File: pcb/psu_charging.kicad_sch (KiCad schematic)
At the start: 22 parts, among them J1 BATT+, J2 GND, J4 VBUS, J6 S2B-PH-K/DNP, J7 GND, J8 124018612112A, U1 AP2112K-3.3, U4 MCP73831/OT

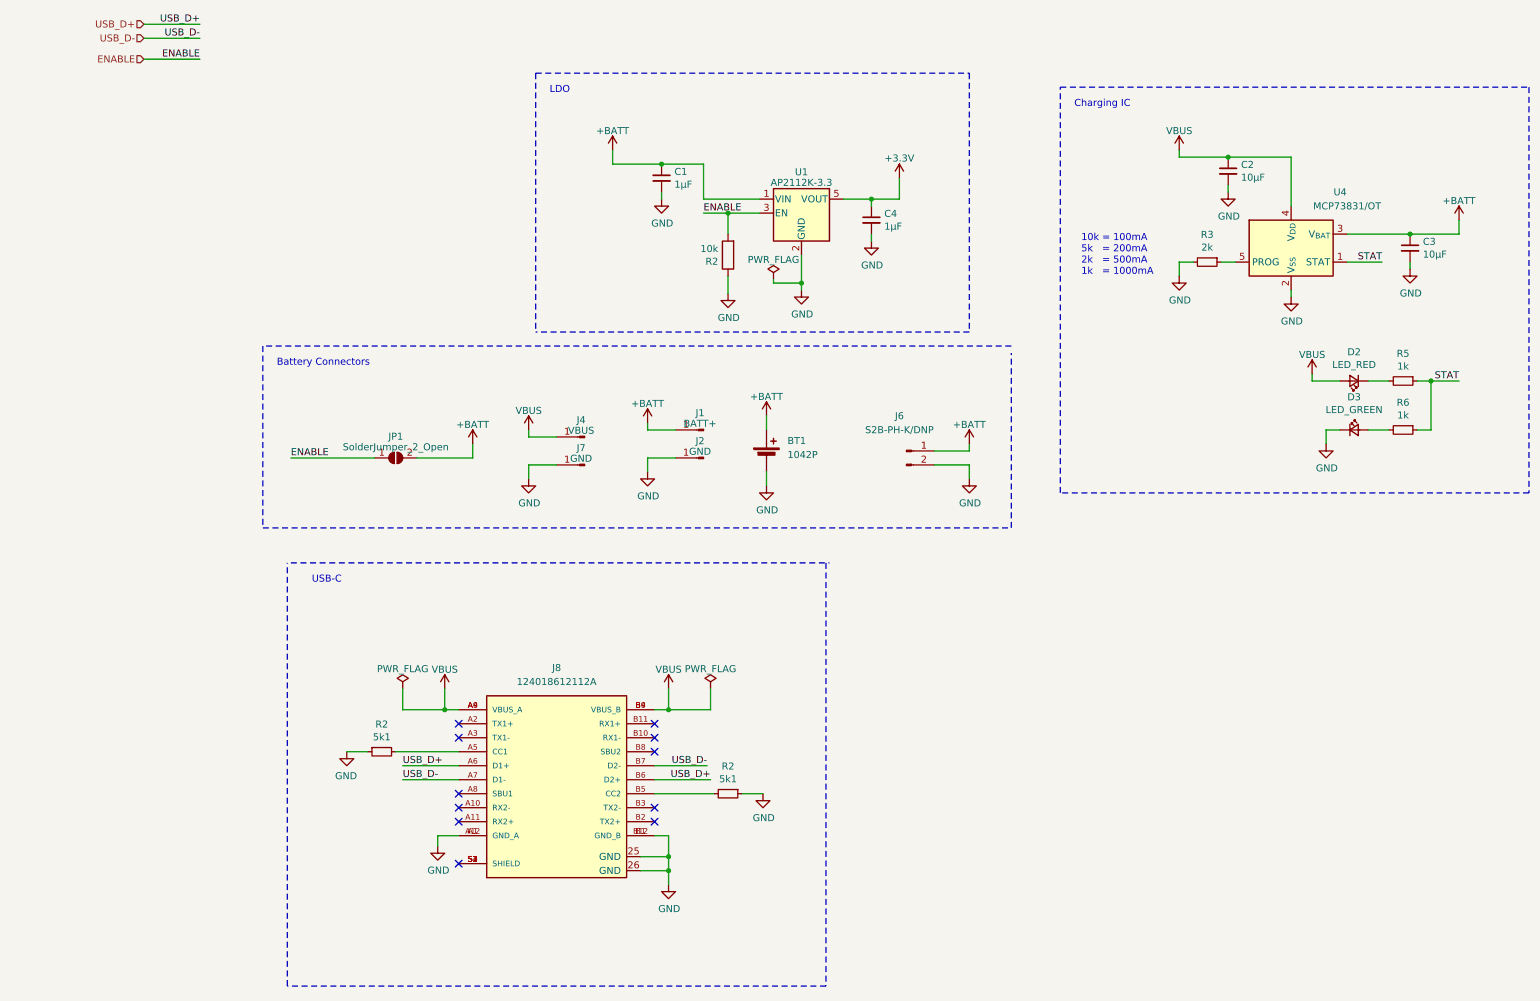
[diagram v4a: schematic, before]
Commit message: re-organise components + added housing data
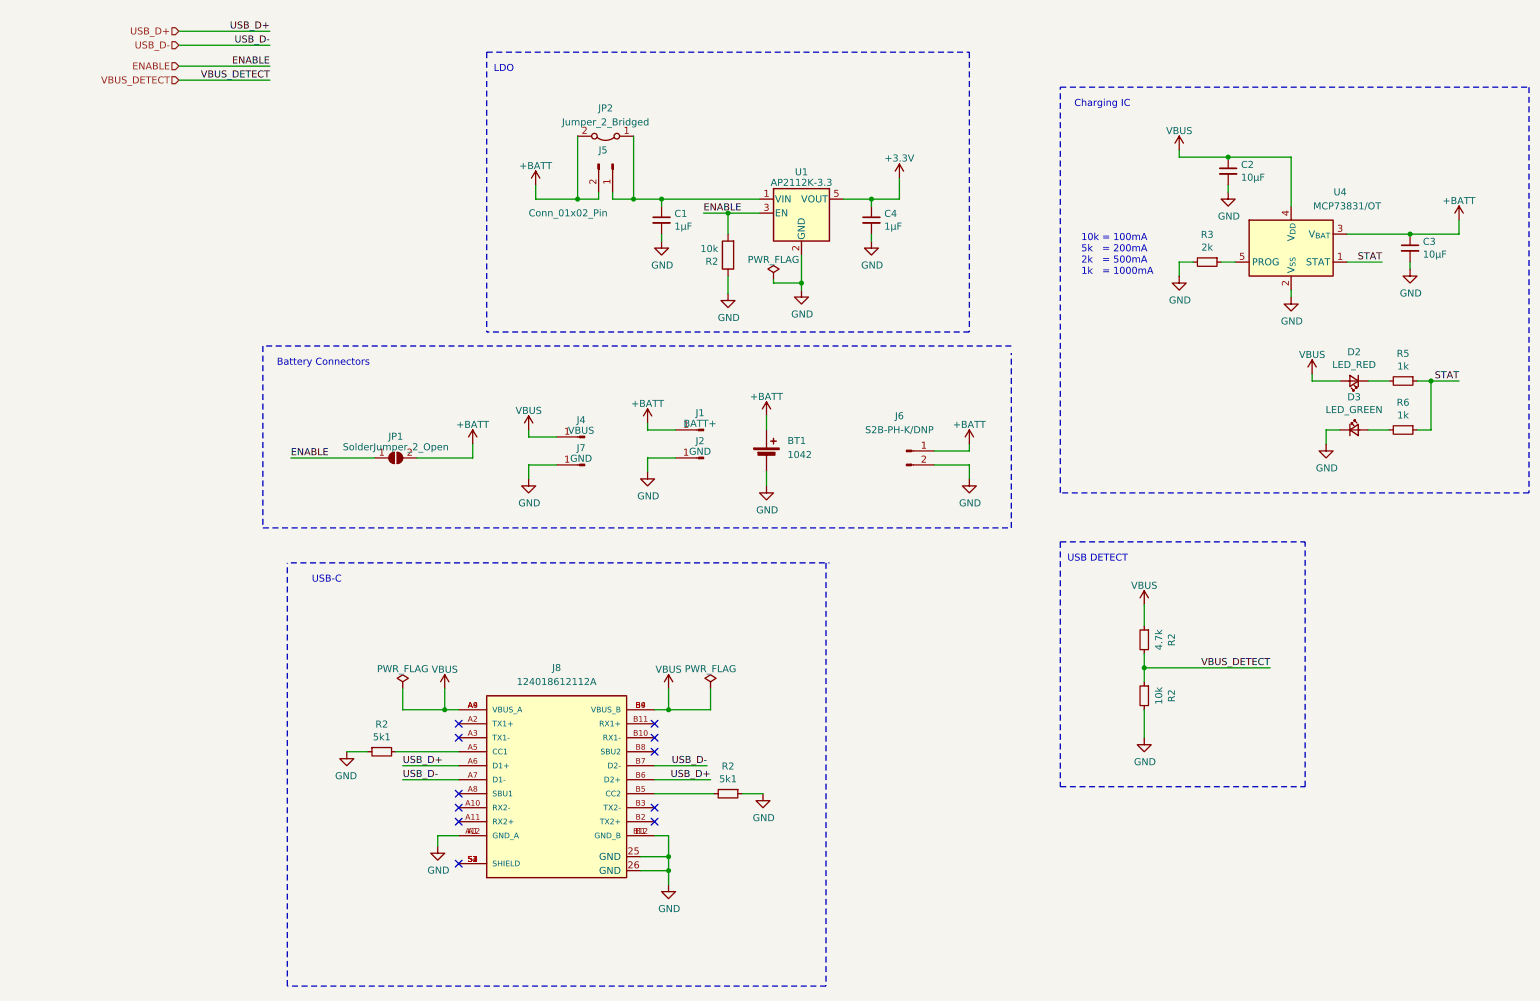
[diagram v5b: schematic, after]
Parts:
- added J5: Conn_01x02_Pin, Connector_PinSocket_2.54mm:PinSocket_1x02_P2.54mm_Vertical, symbol Connector:Conn_01x02_Pin
- added JP2: Jumper_2_Bridged, Jumper:SolderJumper-2_P1.3mm_Bridged_RoundedPad1.0x1.5mm, symbol Jumper:Jumper_2_Bridged
- added R2: 4.7k, Resistor_SMD:R_0603_1608Metric, symbol Device:R_Small
- added R2: 10k, Resistor_SMD:R_0603_1608Metric, symbol Device:R_Small
- BT1: value 1042P -> 1042
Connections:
- net +BATT: now also J5.2 (Pin_2), JP2.2 (B); no longer C1.1, U1.1 (VIN)
- net GND: now also R2.2
- net VBUS: now also R2.1
- new net: C1.1, J5.1 (Pin_1), JP2.1 (A), U1.1 (VIN)
- new net VBUS_DETECT: R2.1, R2.2
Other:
- note added: "USB DETECT"
- moved on the sheet: C1

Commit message: Replaced RP2040 with ESP32 + Schematics + Layouting
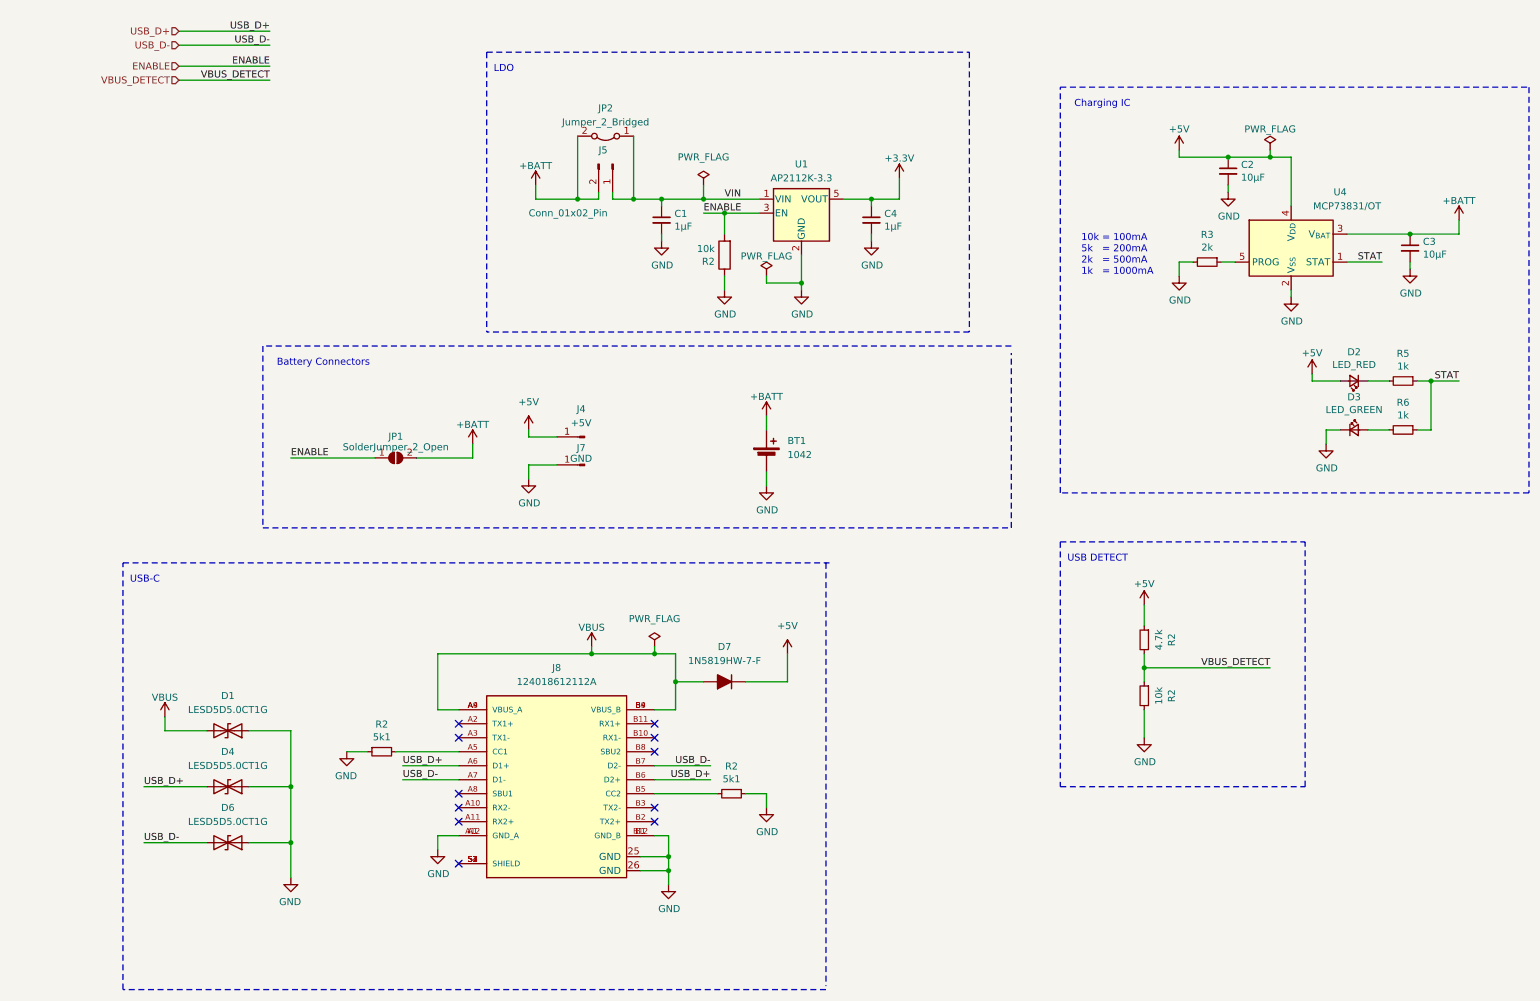
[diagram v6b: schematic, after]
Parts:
- removed J1: BATT+, TestPoint:TestPoint_Pad_2.0x2.0mm, symbol Connector:Conn_01x01_Pin
- removed J2: GND, TestPoint:TestPoint_Pad_2.0x2.0mm, symbol Connector:Conn_01x01_Pin
- removed J6: S2B-PH-K/DNP, Connector_JST:JST_PH_S2B-PH-SM4-TB_1x02-1MP_P2.00mm_Horizontal, symbol Connector:Conn_01x02_Pin
- added D1, D4, D6: LESD5D5.0CT1G, LESD5D5.0CT1G:LESD5D50CT1G, symbol Device:D_TVS
- added D7: 1N5819HW-7-F, 1N5819HW-7-F:SOD3716X145N, symbol Device:D_Filled
- J4: value VBUS -> +5V
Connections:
- net GND: now also D1.1 (A1), D4.1 (A1), D6.1 (A1)
- net USB_D+: now also D4.2 (A2)
- net USB_D-: now also D6.2 (A2)
- net VBUS: now also D1.2 (A2), D7.2 (A); no longer C2.1, D2.2 (A), J4.1 (Pin_1), R2.1, U4.4 (V_{DD})
- net VIN: now reaches C1.1, J5.1 (Pin_1), JP2.1 (A), U1.1 (VIN)
- new net +5V: C2.1, D2.2 (A), D7.1 (K), J4.1 (Pin_1), R2.1, U4.4 (V_{DD})
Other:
- moved on the sheet: R2

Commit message: Removed diode from VBUS to 5V+ and removed 5V+ because it is not needed
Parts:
- removed D7: 1N5819HW-7-F, 1N5819HW-7-F:SOD3716X145N, symbol Device:D_Filled
- J4: value +5V -> VBUS
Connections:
- net +5V is gone; now on net VBUS: C2.1, D2.2 (A), J4.1 (Pin_1), R2.1, U4.4 (V_{DD})

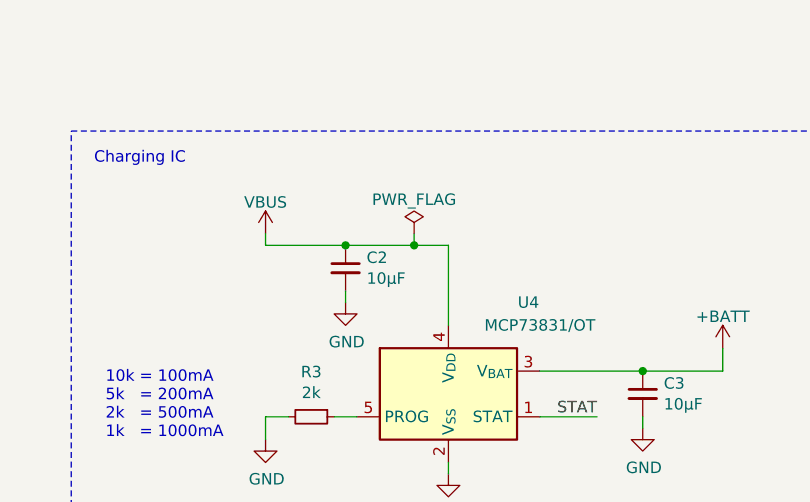
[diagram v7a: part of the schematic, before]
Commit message: Changed net names to match functionallity of active low
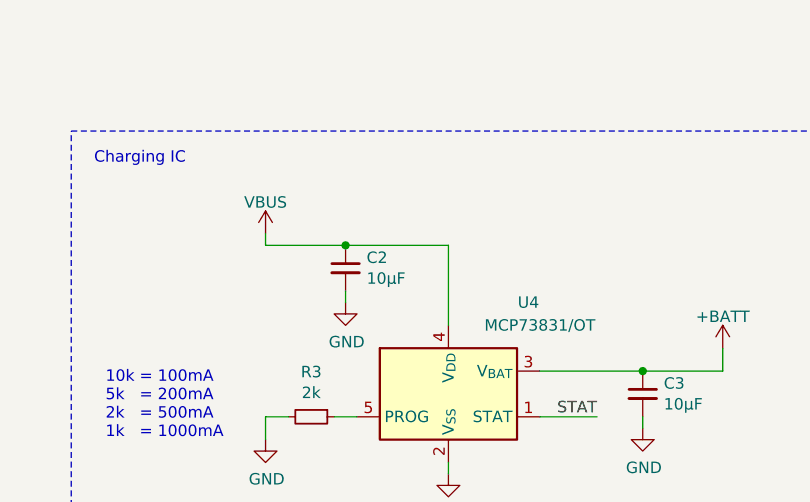
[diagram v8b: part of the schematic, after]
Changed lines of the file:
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@@
   (junction (at 118.11 166.37) (diameter 0) (color 0 0 0 0)
-  )
-  (junction (at 227.33 39.37) (diameter 0) (color 0 0 0 0)
   )
   (junction (at 49.53 153.67) (diameter 0) (color 0 0 0 0)
@@
     (stroke (width 0) (type default))
   )
-  (wire (pts (xy 227.33 39.37) (xy 219.71 39.37))
+  (wire (pts (xy 219.71 39.37) (xy 231.14 39.37))
     (stroke (width 0) (type default))
   )
@@
     (stroke (width 0) (type default))
   )
-  (wire (pts (xy 227.33 38.1) (xy 227.33 39.37))
-    (stroke (width 0) (type default))
-  )
   (wire (pts (xy 49.53 153.67) (xy 49.53 143.51))
     (stroke (width 0) (type default))
@@
   (polyline (pts (xy 274.32 26.67) (xy 274.32 100.33))
     (stroke (width 0) (type dash))
-  )
-  (wire (pts (xy 231.14 39.37) (xy 227.33 39.37))
-    (stroke (width 0) (type default))
   )
   (wire (pts (xy 115.57 149.86) (xy 125.73 149.86))
@@
         )
       )
-    )
-  )
-  (symbol (lib_id "power:PWR_FLAG") (at 227.33 38.1 0) (unit 1)
-    (in_bom yes) (on_board yes) (dnp no)
-    (property "Reference" "#FLG04" (at 227.33 36.195 0)
-      (effects (font (size 1.27 1.27)) hide)
-    )
-    (property "Value" "PWR_FLAG" (at 227.33 34.29 0)
-      (effects (font (size 1.27 1.27)))
-    )
-    (property "Footprint" "" (at 227.33 38.1 0)
-      (effects (font (size 1.27 1.27)) hide)
-    )
-    (property "Datasheet" "~" (at 227.33 38.1 0)
-      (effects (font (size 1.27 1.27)) hide)
-    )
-    (pin "1")
-    (instances
-      (project "rep-trap-pcb"
-        (path "/b363dc8f-4a45-4779-a397-ccb82393dab8/eebb1d37-a01d-4adf-be70-a8e8f9293475/23008b32-6835-495f-a93f-d60d3125c4cb"
-          (reference "#FLG04") (unit 1)
-        )
-      )
